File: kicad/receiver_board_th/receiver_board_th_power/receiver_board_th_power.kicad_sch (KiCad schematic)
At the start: 12 parts, among them J1 B2B 1, J2 B2B 2, J3 Motor 1, J4 Motor 2, J5 Battery Mon, U1 ESP32-C3-SuperMini, U2 Dual H Bridge

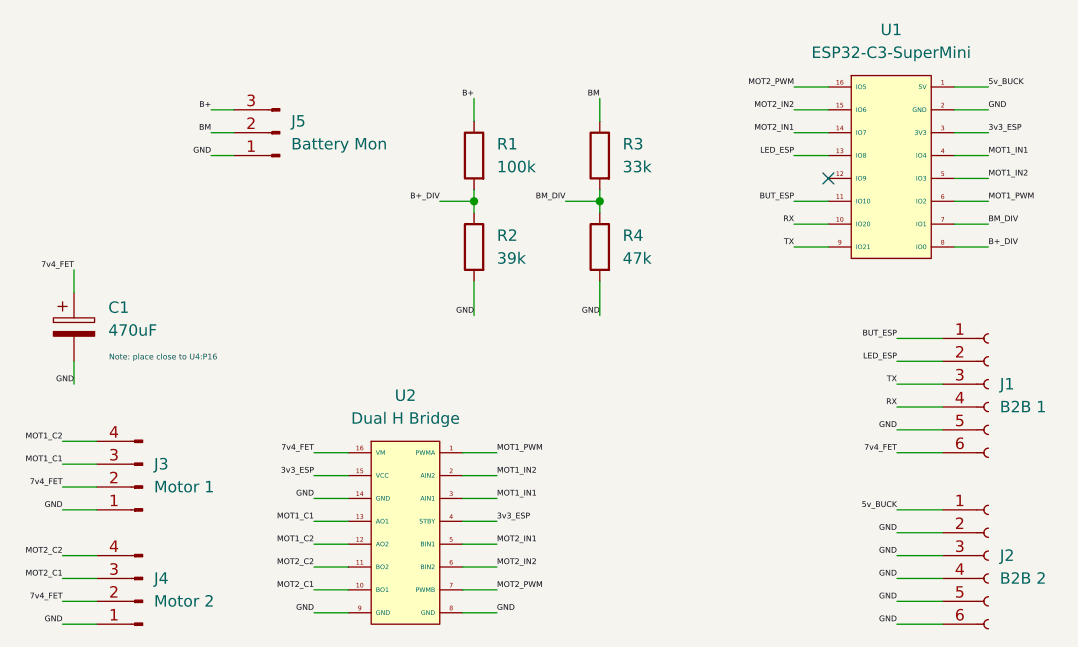
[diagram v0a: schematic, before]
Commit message: Add M2 mounting holes to receiver power board
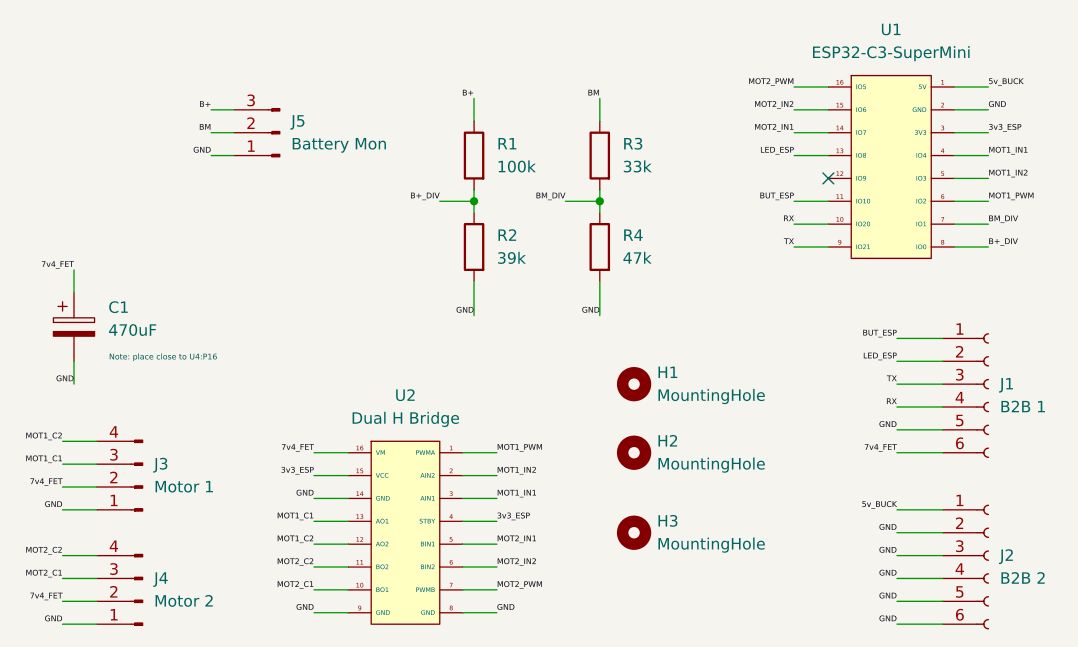
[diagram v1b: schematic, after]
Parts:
- added H1, H2, H3: MountingHole, MountingHole:MountingHole_2.2mm_M2_Pad_TopBottom, symbol Mechanical:MountingHole
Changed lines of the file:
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@@
+	)
+	(symbol
+		(lib_id "Mechanical:MountingHole")
+		(at 195.58 67.31 0)
+		(unit 1)
+		(exclude_from_sim no)
+		(in_bom no)
+		(on_board yes)
+		(dnp no)
+		(fields_autoplaced yes)
+		(property "Reference" "H2"
+			(at 198.12 66.0399 0)
+			(effects
+				(font
+					(size 1.27 1.27)
+				)
+				(justify left)
+			)
+		)
+		(property "Value" "MountingHole"
+			(at 198.12 68.5799 0)
+			(effects
+				(font
+					(size 1.27 1.27)
+				)
+				(justify left)
+			)
+		)
+		(property "Footprint" "MountingHole:MountingHole_2.2mm_M2_Pad_TopBottom"
+			(at 195.58 67.31 0)
+			(effects
+				(font
+					(size 1.27 1.27)
+				)
+				(hide yes)
+			)
+		)
+		(property "Datasheet" "~"
+			(at 195.58 67.31 0)
+			(effects
+				(font
+					(size 1.27 1.27)
+				)
+				(hide yes)
+			)
+		)
+		(property "Description" "Mounting Hole without connection"
+			(at 195.58 67.31 0)
+			(effects
+				(font
+					(size 1.27 1.27)
+				)
+				(hide yes)
+			)
+		)
+		(instances
+			(project "receiver_board_th_power"
+				(path "/c65229a9-37b7-4cd8-a90e-78faaca9b050"
+					(reference "H2")
+					(unit 1)
+				)
+			)
+		)
+	)
+	(symbol
+		(lib_id "Mechanical:MountingHole")
+		(at 195.58 76.2 0)
+		(unit 1)
+		(exclude_from_sim no)
+		(in_bom no)
+		(on_board yes)
+		(dnp no)
+		(fields_autoplaced yes)
+		(property "Reference" "H3"
+			(at 198.12 74.9299 0)
+			(effects
+				(font
+					(size 1.27 1.27)
+				)
+				(justify left)
+			)
+		)
+		(property "Value" "MountingHole"
+			(at 198.12 77.4699 0)
+			(effects
+				(font
+					(size 1.27 1.27)
+				)
+				(justify left)
+			)
+		)
+		(property "Footprint" "MountingHole:MountingHole_2.2mm_M2_Pad_TopBottom"
+			(at 195.58 76.2 0)
+			(effects
+				(font
+					(size 1.27 1.27)
+				)
+				(hide yes)
+			)
+		)
+		(property "Datasheet" "~"
+			(at 195.58 76.2 0)
+			(effects
+				(font
+					(size 1.27 1.27)
+				)
+				(hide yes)
+			)
+		)
+		(property "Description" "Mounting Hole without connection"
+			(at 195.58 76.2 0)
+			(effects
+				(font
+					(size 1.27 1.27)
+				)
+				(hide yes)
+			)
+		)
+		(instances
+			(project "receiver_board_th_power"
+				(path "/c65229a9-37b7-4cd8-a90e-78faaca9b050"
+					(reference "H3")
+					(unit 1)
+				)
+			)
+		)
 	)
 	(symbol
@@
 					(unit 1)
 				)
+			)
+		)
+	)
+	(symbol
+		(lib_id "Mechanical:MountingHole")
+		(at 195.58 59.69 0)
+		(unit 1)
+		(exclude_from_sim no)
+		(in_bom no)
+		(on_board yes)
+		(dnp no)
+		(fields_autoplaced yes)
+		(property "Reference" "H1"
+			(at 198.12 58.4199 0)
+			(effects
+				(font
+					(size 1.27 1.27)
+				)
+				(justify left)
+			)
+		)
+		(property "Value" "MountingHole"
+			(at 198.12 60.9599 0)
+			(effects
+				(font
+					(size 1.27 1.27)
+				)
+				(justify left)
+			)
+		)
+		(property "Footprint" "MountingHole:MountingHole_2.2mm_M2_Pad_TopBottom"
+			(at 195.58 59.69 0)
+			(effects
+				(font
+					(size 1.27 1.27)
+				)
+				(hide yes)
+			)
+		)
+		(property "Datasheet" "~"
+			(at 195.58 59.69 0)
+			(effects
+				(font
+					(size 1.27 1.27)
+				)
+				(hide yes)
+			)
+		)
+		(property "Description" "Mounting Hole without connection"
+			(at 195.58 59.69 0)
+			(effects
+				(font
+					(size 1.27 1.27)
+				)
+				(hide yes)
+			)
+		)
+		(instances
+			(project ""
+				(path "/c65229a9-37b7-4cd8-a90e-78faaca9b050"
+					(reference "H1")
+					(unit 1)
+				)
